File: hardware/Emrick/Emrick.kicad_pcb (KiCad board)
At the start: 4 copper layers, 41.5 x 71.7 mm, 87 parts, among them J1 LED_STRIP_CONNECTOR, J2 UFL, J3 Conn_02x05_Odd_Even, J4 BATT_CONN, P1 USB_C_Plug_USB2.0, Q1 Q_NPN_DGS, Q2 Q_NPN_DGS, Q3 Q_NPN_DGS, SW1 SW_SPST, SW2 SW_MEC_5E (RESET)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

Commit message: first pass at pcb
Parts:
- R3: value R -> 0
- U6: value BQ24072RGTR -> BQ24072
- moved Q1 0.20 mm to (97.2, 35.7)
- moved Q2 0.20 mm to (95.3, 35.7)
- moved Q3 0.10 mm to (99.3, 35.6)
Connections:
- U1 pad 11: GND -> unconnected-(U1-Pad11)
- U1 pad 12: GND -> unconnected-(U1-Pad12)
- U1 pad 13: GND -> unconnected-(U1-Pad13)
- U1 pad 14: GND -> unconnected-(U1-Pad14)
- U1 pad 15: GND -> unconnected-(U1-Pad15)
- U1 pad 16: GND -> unconnected-(U1-Pad16)
- U1 pad 17: GND -> unconnected-(U1-Pad17)
- U2 pad GND: (no net) -> GND
- U2 pad V: (no net) -> GND
- U3 pad V: (no net) -> GND
- U6 pad V: (no net) -> GND
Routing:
- net GND: track 97.8 -> 105.1 mm, vias 85 -> 84
- net VDDS: track 133.5 -> 132.3 mm, vias 15 -> 14
- net BBReg_5V: vias 2 -> 1
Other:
- board size 41.5 x 71.7 mm -> 41.5 x 71.5 mm
- board text added: "Emrick rev 1 10/19/2022 Sam Dlott Erik Duxstad Zareef Huq Hamza Kamel ECE477 Fall 22 Group 2"

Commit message: rev 1 of board
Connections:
- SW2 pad 2: unconnected-(SW2-Pad2) -> GND
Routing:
- net GND: track 105.1 -> 110.9 mm
- net unconnected-(SW2-Pad2): track 5.76 -> 0.00 mm

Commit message: fixed PCB gremlins
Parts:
- removed C13: 0.1 uF, Capacitor_SMD:C_0402_1005Metric
- removed C14: 4.7 uF, Capacitor_SMD:C_0402_1005Metric
- C19: value 3pF -> 2.7pF
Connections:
- J4 pad 1: Net-(J4-Pad1) -> GND
- J4 pad 3: GND -> Net-(J4-Pad3)
- SW1 pad 2: Net-(J4-Pad1) -> Net-(J4-Pad3)
- U2 pad 7: UART_RX -> UART_TX
- U2 pad 8: UART_TX -> UART_RX
- U2 pad GND: GND -> (no net)
- U2 pad V: GND -> (no net)
- U3 pad V: GND -> (no net)
- U4 pad 25: UART_RX -> UART_TX
- U4 pad 26: UART_TX -> UART_RX
- U4 pad 6: VDDS -> Net-(U4-Pad6)
- U4 pad 7: VDDS -> Net-(U4-Pad6)
- U6 pad V: GND -> (no net)
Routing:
- net VDDS: track 132.3 -> 121.9 mm
- net Net-(J4-Pad3): track 0.00 -> 7.86 mm
- net Net-(J4-Pad1): track 6.96 -> 0.00 mm
- net Net-(U4-Pad6): track 0.00 -> 2.59 mm
- net GND: track 110.9 -> 108.6 mm, vias 84 -> 83
- net UART_TX: track 14.2 -> 16.1 mm, vias 0 -> 2
- net UART_RX: track 16.1 -> 14.2 mm, vias 2 -> 0

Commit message: modifications to pcb
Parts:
- C23: value 0.1uF -> 100pF
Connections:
- U4 pad 6: Net-(U4-Pad6) -> unconnected-(U4-Pad6)
- U4 pad 7: Net-(U4-Pad6) -> VDDS
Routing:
- net VDDS: track 121.9 -> 124.8 mm
- net Net-(U4-Pad6): track 2.59 -> 0.00 mm
- net BAT_TS: track 11.1 -> 10.3 mm
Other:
- board text added: "*"

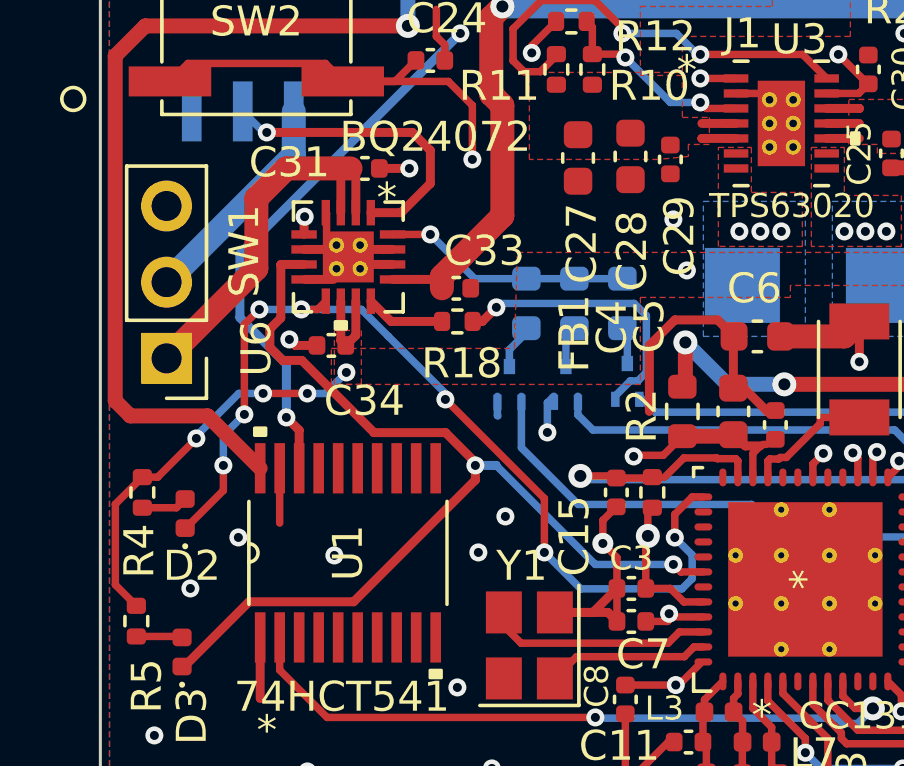
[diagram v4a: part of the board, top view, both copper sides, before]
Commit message: added bypass diode for battery
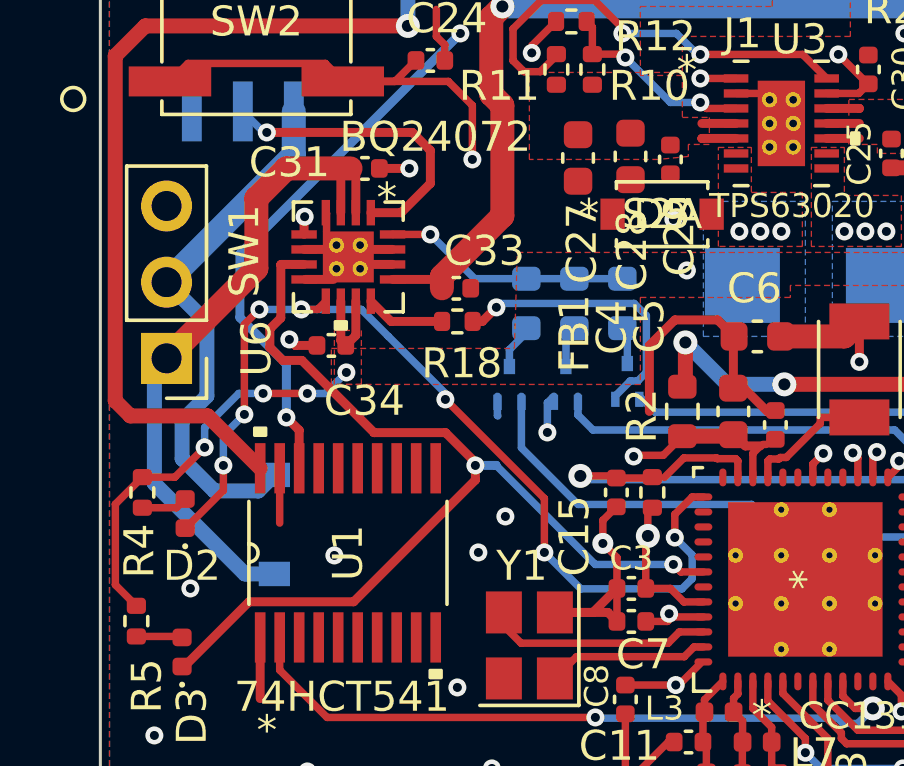
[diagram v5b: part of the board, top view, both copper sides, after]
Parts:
- added D5: S2A, Emrick Footprints:PMEG120G20ELRX, F.Cu at (100.4, 30.0)
- added D5: S2A, Emrick Footprints:PMEG120G20ELRX, B.Cu at (87.5, 40.4)
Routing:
- net Net-(J4-Pad3): track 7.45 -> 18.0 mm
- net VBAT: track 13.0 -> 22.5 mm
- net GND: vias 83 -> 82

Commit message: some work on pcb and schematic
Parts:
- added C13: ?, Capacitor_SMD:C_0402_1005Metric, F.Cu at (101.9, 63.6)
- added L9: ?, Inductor_SMD:L_0402_1005Metric, F.Cu at (102.9, 64.8)
- C12: value 100pF -> ?
- SW1: footprint Connector_PinHeader_2.54mm:PinHeader_1x03_P2.54mm_Vertical -> switch:SW-TH_3P-P4.70_L11.1-W12.7
- moved D5 20.0 mm to (86.1, 44.1)
- moved U1 15.6 mm to (89.2, 56.9)
- moved SW1 12.8 mm to (90.7, 45.7), turned to -90 degrees
- moved D3 8.23 mm to (85.7, 36.5)
- moved R5 8.23 mm to (84.2, 35.5)
- moved D2 8.23 mm to (85.8, 31.9)
- moved R4 8.23 mm to (84.4, 31.2)
- moved AE1 2.47 mm to (102.4, 79.9)
- moved C17 2.47 mm to (102.4, 66.5)
- moved D5 2.23 mm to (87.5, 42.6), turned to -90 degrees
- moved J4 1.86 mm to (86.7, 25.0), turned to 180 degrees
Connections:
- C25 pad 2: VDDS -> VBAT
- C26 pad 2: VDDS -> VBAT
- D5 pad 2: Net-(J4-Pad3) -> Net-(D5-Pad2)
- J4 pad 3: Net-(J4-Pad3) -> Net-(D5-Pad2)
- SW1 pad 2: Net-(J4-Pad3) -> Net-(D5-Pad2)
- U3 pad 10: VDDS -> VBAT
- U3 pad 11: VDDS -> VBAT
- U3 pad 12: VDDS -> VBAT
- U4 pad 6: unconnected-(U4-Pad6) -> VDDS
- U4 pad 7: VDDS -> VBAT
- U6 pad 10: VDDS -> unconnected-(U6-Pad10)
- U6 pad 11: VDDS -> unconnected-(U6-Pad11)
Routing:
- net Net-(D5-Pad2): track 0.00 -> 29.3 mm
- net Net-(J4-Pad3): track 18.0 -> 0.00 mm
- net VDDS: track 125.2 -> 112.5 mm, vias 14 -> 13
- net BAT_PGOOD: track 34.1 -> 21.9 mm
- net LED_DATA_3V: track 23.5 -> 11.2 mm
- net BBReg_5V: track 46.7 -> 40.9 mm
- net BAT_TS: track 10.3 -> 15.3 mm
- net BAT_CHG: track 32.6 -> 28.0 mm, vias 7 -> 5
- net GND: track 108.6 -> 104.8 mm, vias 82 -> 61
- net VBAT: track 22.5 -> 26.0 mm, vias 0 -> 1
- net Net-(C13-Pad1): track 1.05 -> 3.45 mm
- net LED_DATA_5V: track 29.9 -> 28.7 mm, vias 2 -> 1
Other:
- board size 41.5 x 71.5 mm -> 41.5 x 74.2 mm

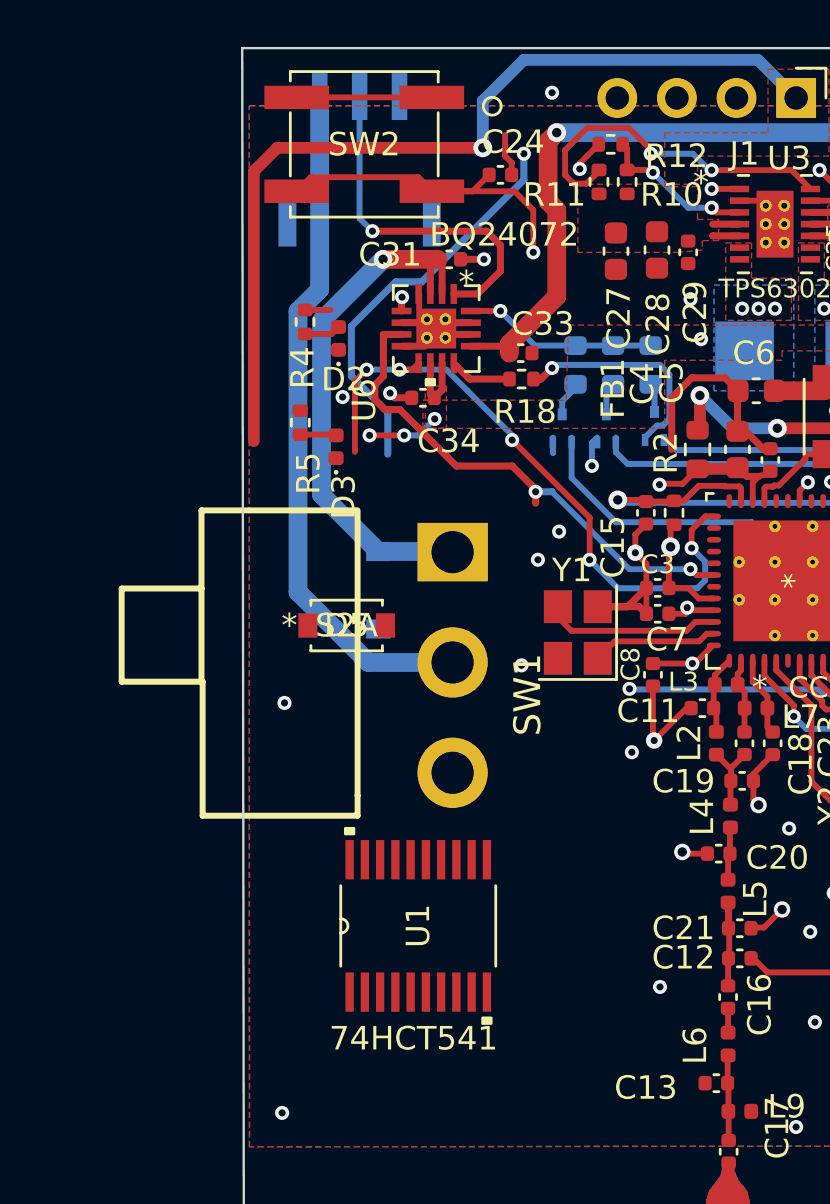
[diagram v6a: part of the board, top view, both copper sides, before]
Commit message: update pcb with preliminary board revisions
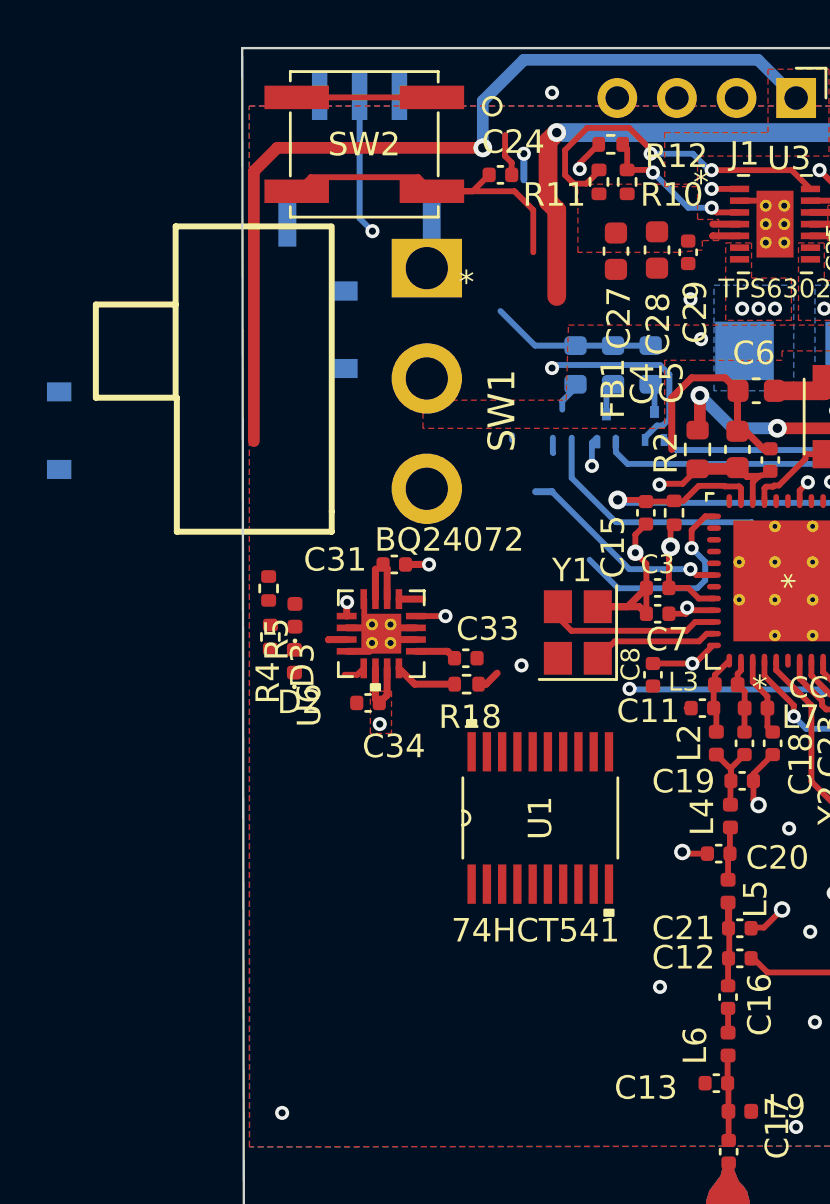
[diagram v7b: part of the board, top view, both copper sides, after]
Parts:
- removed Q2: Q_NPN_DGS, Emrick Footprints:DTC143ZMT2L
- D5: moved to B.Cu
- moved D5 15.2 mm to (73.9, 35.8)
- moved D2 13.9 mm to (83.9, 45.6)
- moved R4 13.5 mm to (82.9, 44.6)
- moved U6 13.2 mm to (87.6, 44.5)
- moved C31 13.2 mm to (88.2, 41.5)
- moved C33 13.2 mm to (91.2, 45.5)
- moved C34 13.2 mm to (87.1, 47.4)
- moved R18 13.2 mm to (91.3, 46.6)
- moved D5 12.6 mm to (86.1, 31.5), turned to -90 degrees
- moved SW1 12.1 mm to (89.6, 33.6)
- moved D3 7.39 mm to (83.9, 43.7)
- moved R5 7.19 mm to (82.8, 42.5)
- moved U1 6.94 mm to (94.4, 52.3)
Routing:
- net Net-(D5-Pad2): track 29.3 -> 0.00 mm
- net VBAT: track 26.0 -> 6.10 mm, vias 1 -> 0
- net BAT_CHG: track 28.0 -> 10.3 mm, vias 5 -> 1
- net LED_DATA_5V: track 28.7 -> 12.6 mm
- net BAT_PGOOD: track 21.9 -> 9.85 mm, vias 2 -> 1
- net VDDS: track 112.5 -> 102.5 mm, vias 13 -> 11
- net BAT_TS: track 15.3 -> 7.08 mm
- net GND: track 104.8 -> 99.5 mm, vias 61 -> 54
- net VBUS: track 41.2 -> 37.9 mm
- net Net-(D2-Pad2): track 1.55 -> 0.00 mm
- net Net-(D3-Pad2): track 1.54 -> 0.00 mm
- net WMCU_RESET: vias 3 -> 2

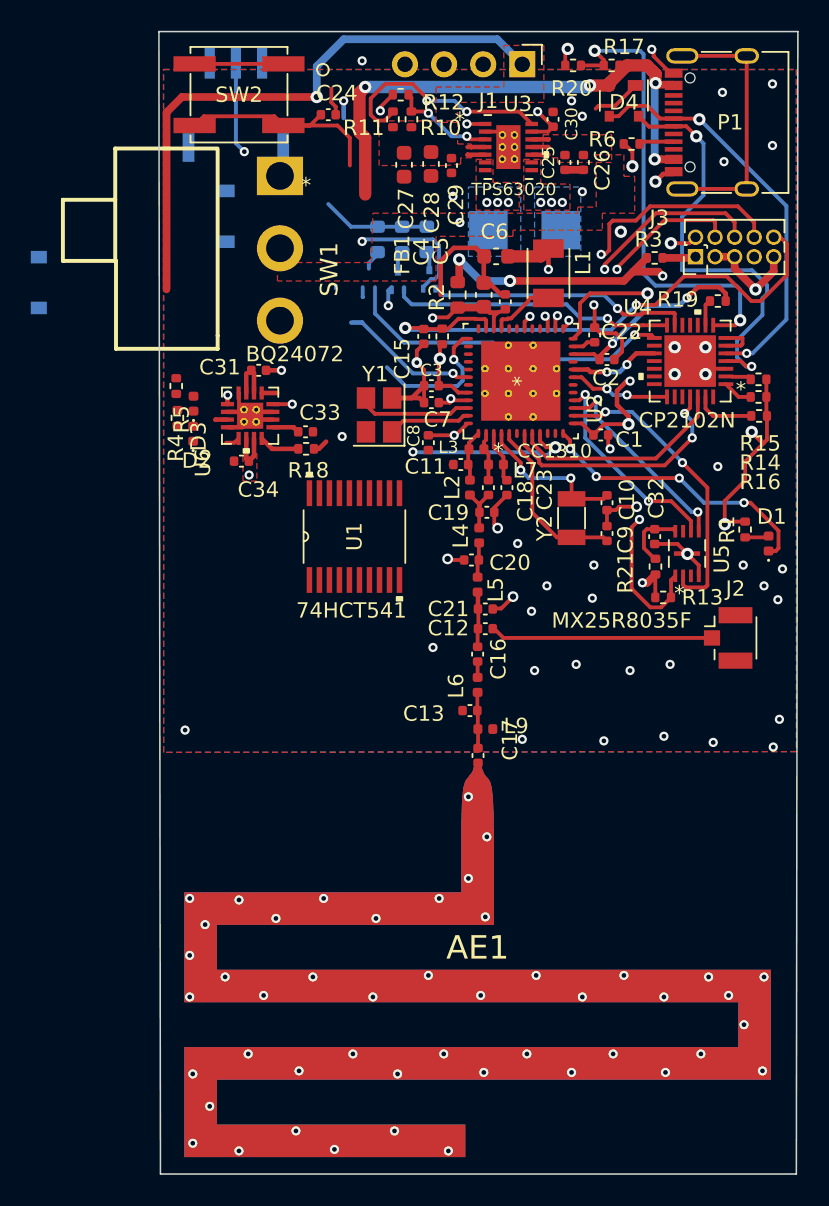
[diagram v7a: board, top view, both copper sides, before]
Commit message: revert unecessary changes to PCB
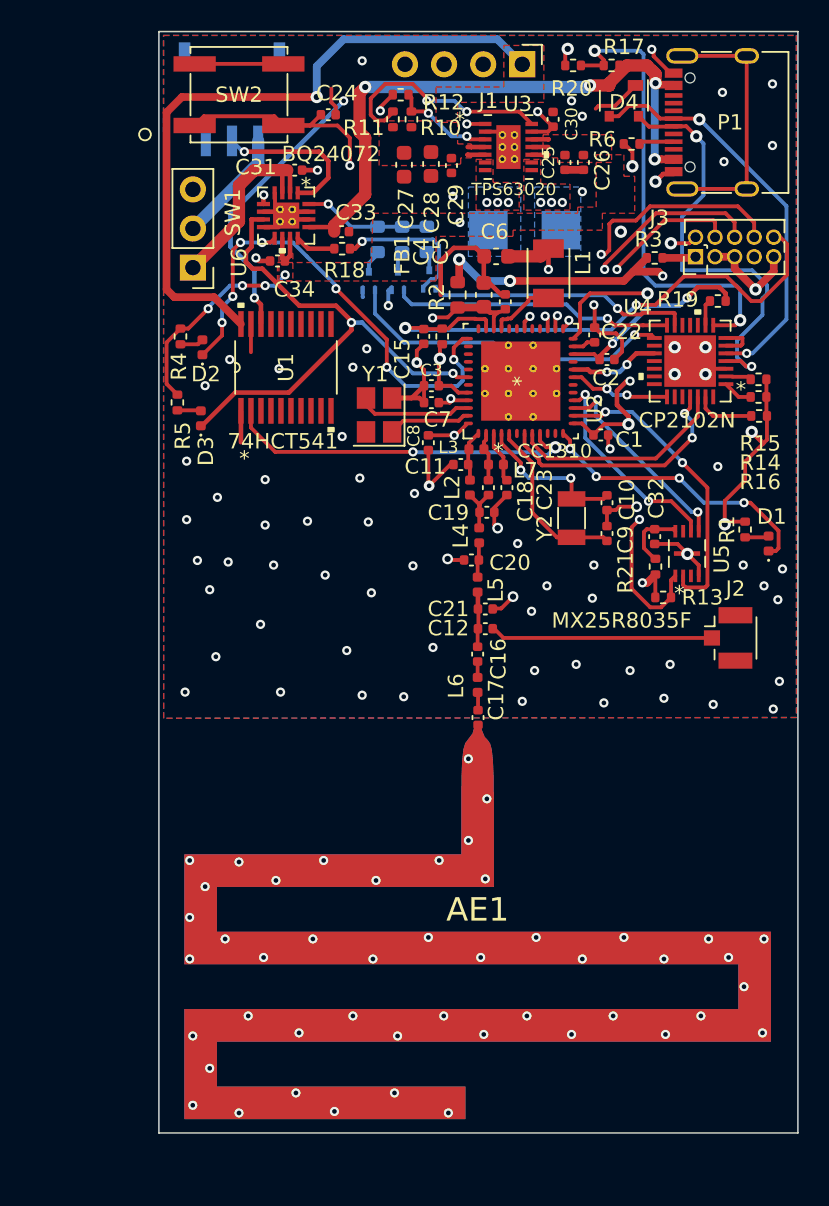
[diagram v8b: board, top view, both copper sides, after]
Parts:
- removed C13: ?, Capacitor_SMD:C_0402_1005Metric
- removed D5 (x2): S2A, Emrick Footprints:PMEG120G20ELRX
- removed L9: ?, Inductor_SMD:L_0402_1005Metric
- added Q2: Q_NPN_DGS, Emrick Footprints:DTC143ZMT2L, B.Cu at (95.3, 35.7)
- C12: value ? -> 100pF
- SW1: footprint switch:SW-TH_3P-P4.70_L11.1-W12.7 -> Connector_PinHeader_2.54mm:PinHeader_1x03_P2.54mm_Vertical
- moved U6 13.2 mm to (90.0, 31.4)
- moved C31 13.2 mm to (90.5, 28.5)
- moved C33 13.2 mm to (93.6, 32.5)
- moved C34 13.2 mm to (89.4, 34.4)
- moved R18 13.2 mm to (93.6, 33.6)
- moved U1 11.9 mm to (90.0, 41.3)
- moved SW1 5.79 mm to (83.9, 34.8), turned to 180 degrees
- moved D2 5.65 mm to (84.5, 40.0)
- moved R4 5.29 mm to (83.1, 39.3)
- moved AE1 2.47 mm to (102.4, 77.4)
- moved C17 2.47 mm to (102.4, 64.1)
- moved J4 1.86 mm to (86.4, 23.2), turned to 0 degrees
- moved R5 1.07 mm to (82.9, 43.6)
- moved D3 1.06 mm to (84.4, 44.6)
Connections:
- C25 pad 2: VBAT -> VDDS
- C26 pad 2: VBAT -> VDDS
- U3 pad 10: VBAT -> VDDS
- U3 pad 11: VBAT -> VDDS
- U3 pad 12: VBAT -> VDDS
- U4 pad 6: VDDS -> unconnected-(U4-Pad6)
- U4 pad 7: VBAT -> VDDS
- U6 pad 10: unconnected-(U6-Pad10) -> VDDS
- U6 pad 11: unconnected-(U6-Pad11) -> VDDS
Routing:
- net BAT_PGOOD: track 9.85 -> 34.1 mm, vias 1 -> 2
- net BAT_CHG: track 10.3 -> 32.6 mm, vias 1 -> 7
- net VDDS: track 102.5 -> 124.8 mm, vias 11 -> 14
- net LED_DATA_5V: track 12.6 -> 29.9 mm, vias 1 -> 2
- net LED_DATA_3V: track 11.2 -> 23.5 mm
- net GND: track 99.5 -> 108.6 mm, vias 54 -> 83
- net Net-(J4-Pad3): track 0.00 -> 7.45 mm
- net VBAT: track 6.10 -> 13.0 mm
- net BBReg_5V: track 40.9 -> 46.7 mm
- net VBUS: track 37.9 -> 41.2 mm
- net BAT_TS: track 7.08 -> 10.3 mm
- net Net-(C17-Pad1): track 3.45 -> 1.05 mm
- net Net-(D2-Pad2): track 0.00 -> 1.55 mm
- net Net-(D3-Pad2): track 0.00 -> 1.54 mm
- net WMCU_RESET: vias 2 -> 3
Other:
- board size 41.5 x 74.2 mm -> 41.5 x 71.5 mm
